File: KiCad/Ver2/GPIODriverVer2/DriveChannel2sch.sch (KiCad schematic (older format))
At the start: 19 parts, among them Q3 2N3904, Q4 MMBT5401, Q5 MMBT5551L, U5 LTV-357T

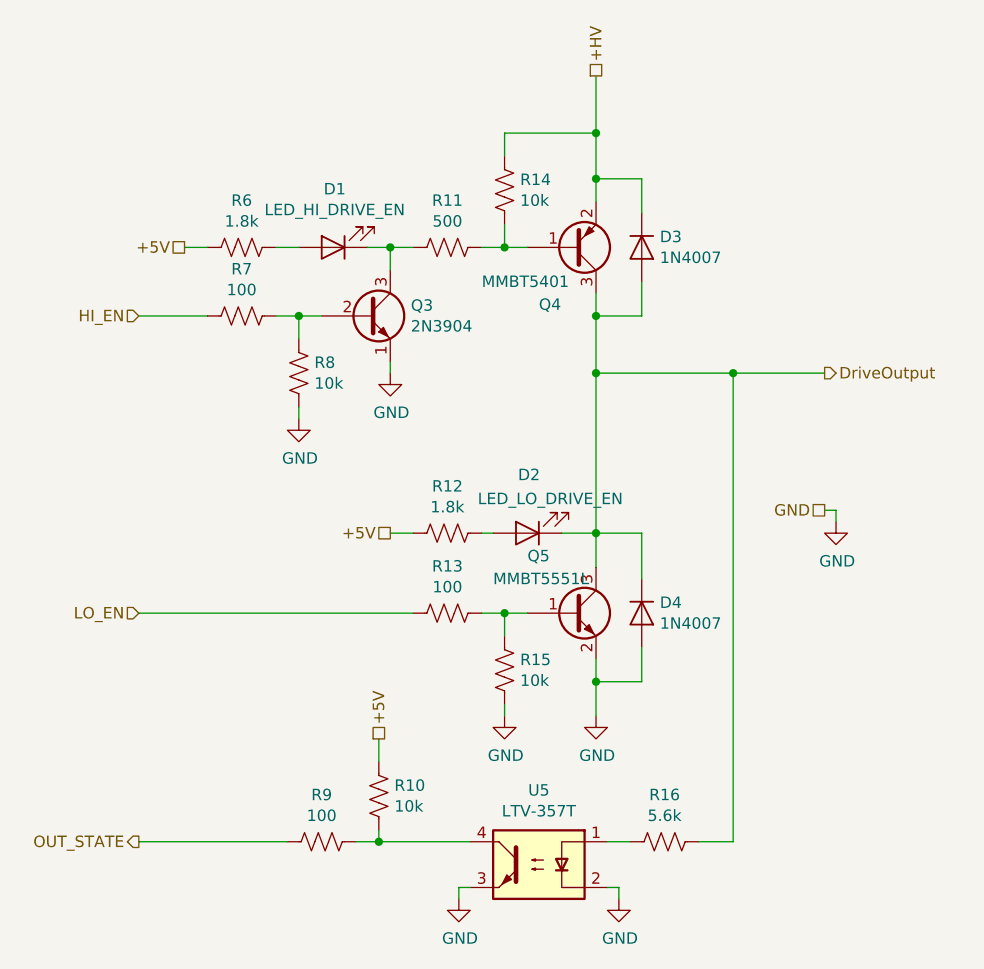
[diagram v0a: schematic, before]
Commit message: Add sheets for output drive channels.
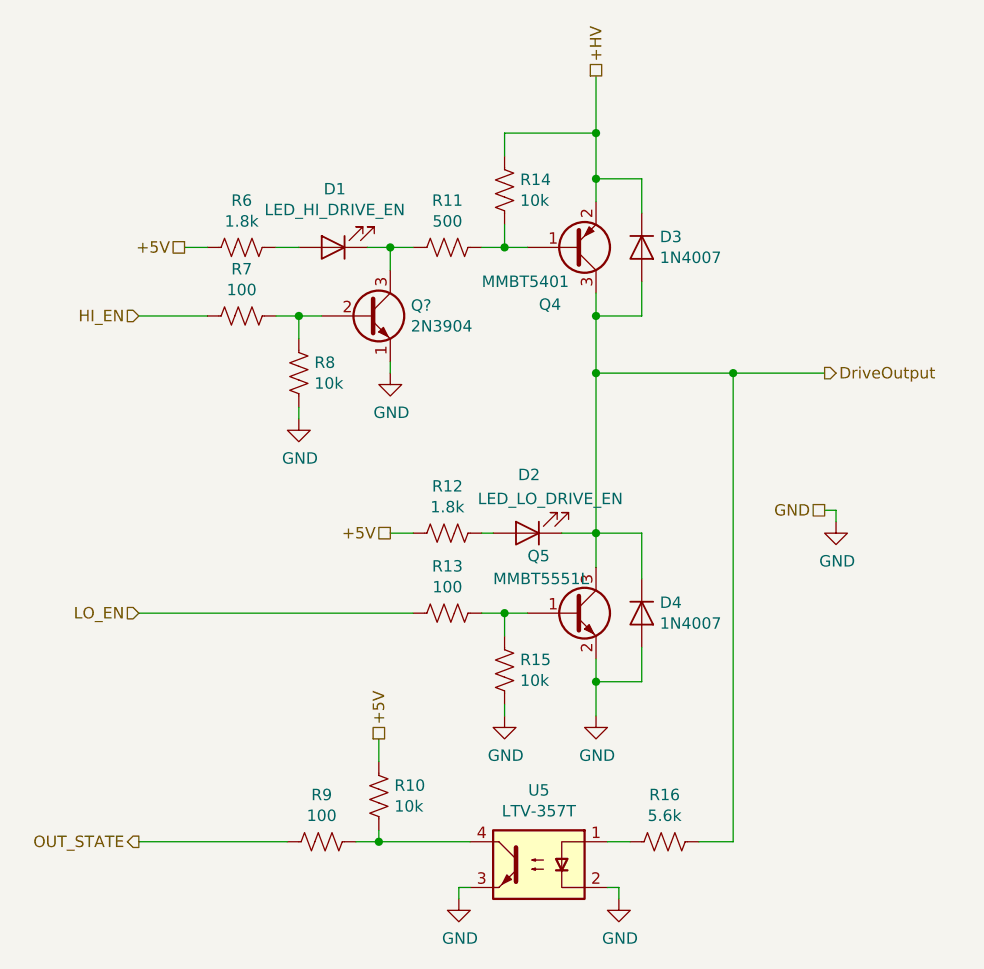
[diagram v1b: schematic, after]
